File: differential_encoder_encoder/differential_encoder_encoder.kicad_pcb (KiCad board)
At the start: 2 copper layers, 51.8 x 46.2 mm, 15 parts, among them J101 RJ45_LED_Shielded, J102 Conn_02x08_Odd_Even, U101 MAX489E, U102 MAX489E, U103 MAX489E

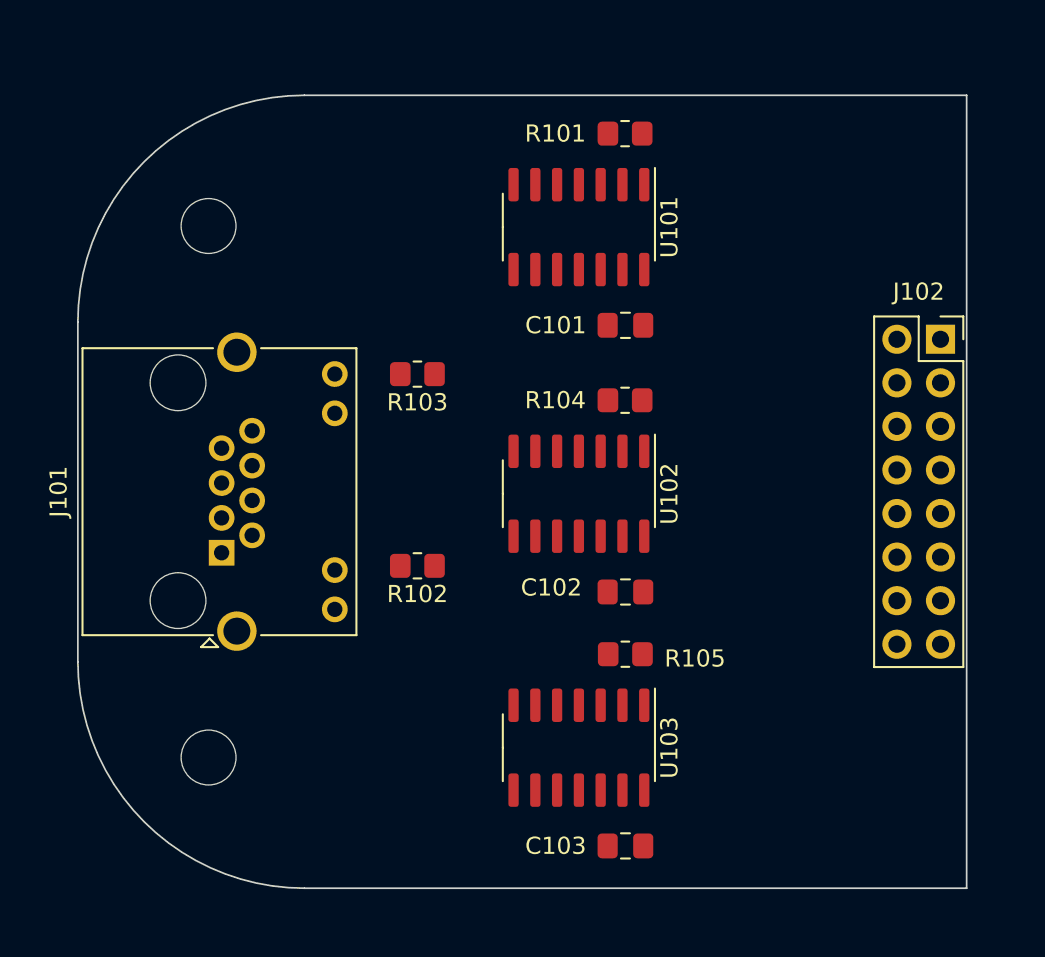
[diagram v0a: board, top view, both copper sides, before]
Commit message: finished the encoder tracing
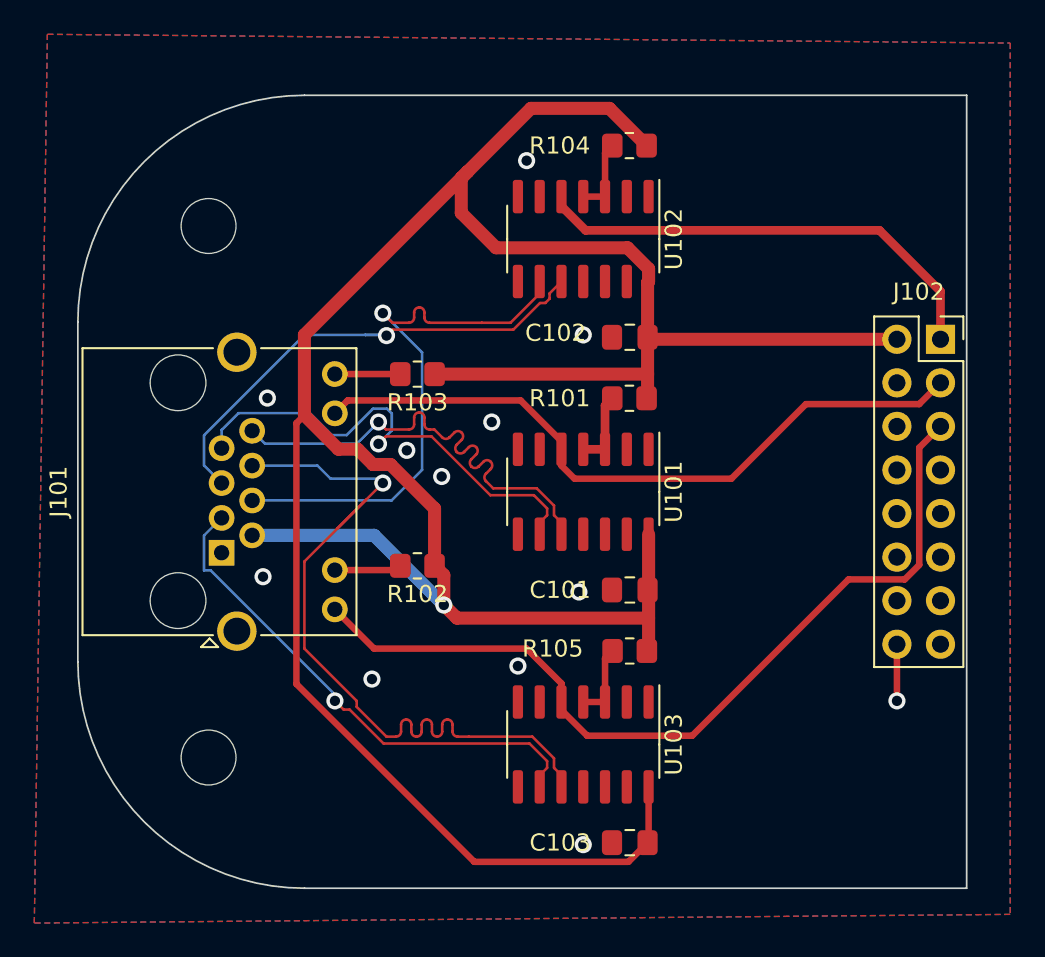
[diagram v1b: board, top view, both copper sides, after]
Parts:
- R105: value locked -> 100
- moved C101 15.4 mm to (173.9, 71.5)
- moved U101 15.4 mm to (171.2, 65.8)
- moved R101 15.4 mm to (173.9, 60.3)
- moved C102 14.8 mm to (173.9, 56.8)
- moved R104 14.8 mm to (173.9, 45.6)
- moved U102 14.8 mm to (171.2, 51.1)
- moved R105 0.32 mm to (173.9, 75.1)
- moved C103 0.32 mm to (173.9, 86.2)
- moved U103 0.32 mm to (171.2, 80.5)
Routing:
- net +5V: track 0.00 -> 172.5 mm, vias 0 -> 1
- net I: track 0.00 -> 50.7 mm
- net i-: track 0.00 -> 45.6 mm, vias 0 -> 1
- net A: track 0.00 -> 40.7 mm
- net b+: track 0.00 -> 32.7 mm, vias 0 -> 1
- net i+: track 0.00 -> 30.0 mm, vias 0 -> 1
- net b-: track 0.00 -> 29.2 mm, vias 0 -> 1
- net a-: track 0.00 -> 28.7 mm, vias 0 -> 1
- net a+: track 0.00 -> 28.2 mm, vias 0 -> 1
- net B: track 0.00 -> 27.5 mm
- net Net-(U103-DE): track 0.00 -> 4.43 mm
- net Net-(U102-DE): track 0.00 -> 4.42 mm
- net Net-(U101-DE): track 0.00 -> 4.42 mm
- net Net-(J101-Pad10): track 0.00 -> 3.92 mm
- net Net-(J101-Pad12): track 0.00 -> 3.82 mm
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- added copper zone on B.Cu, net GND
- added copper zone on F.Cu, net GND
